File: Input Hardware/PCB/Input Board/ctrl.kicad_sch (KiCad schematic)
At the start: 38 parts

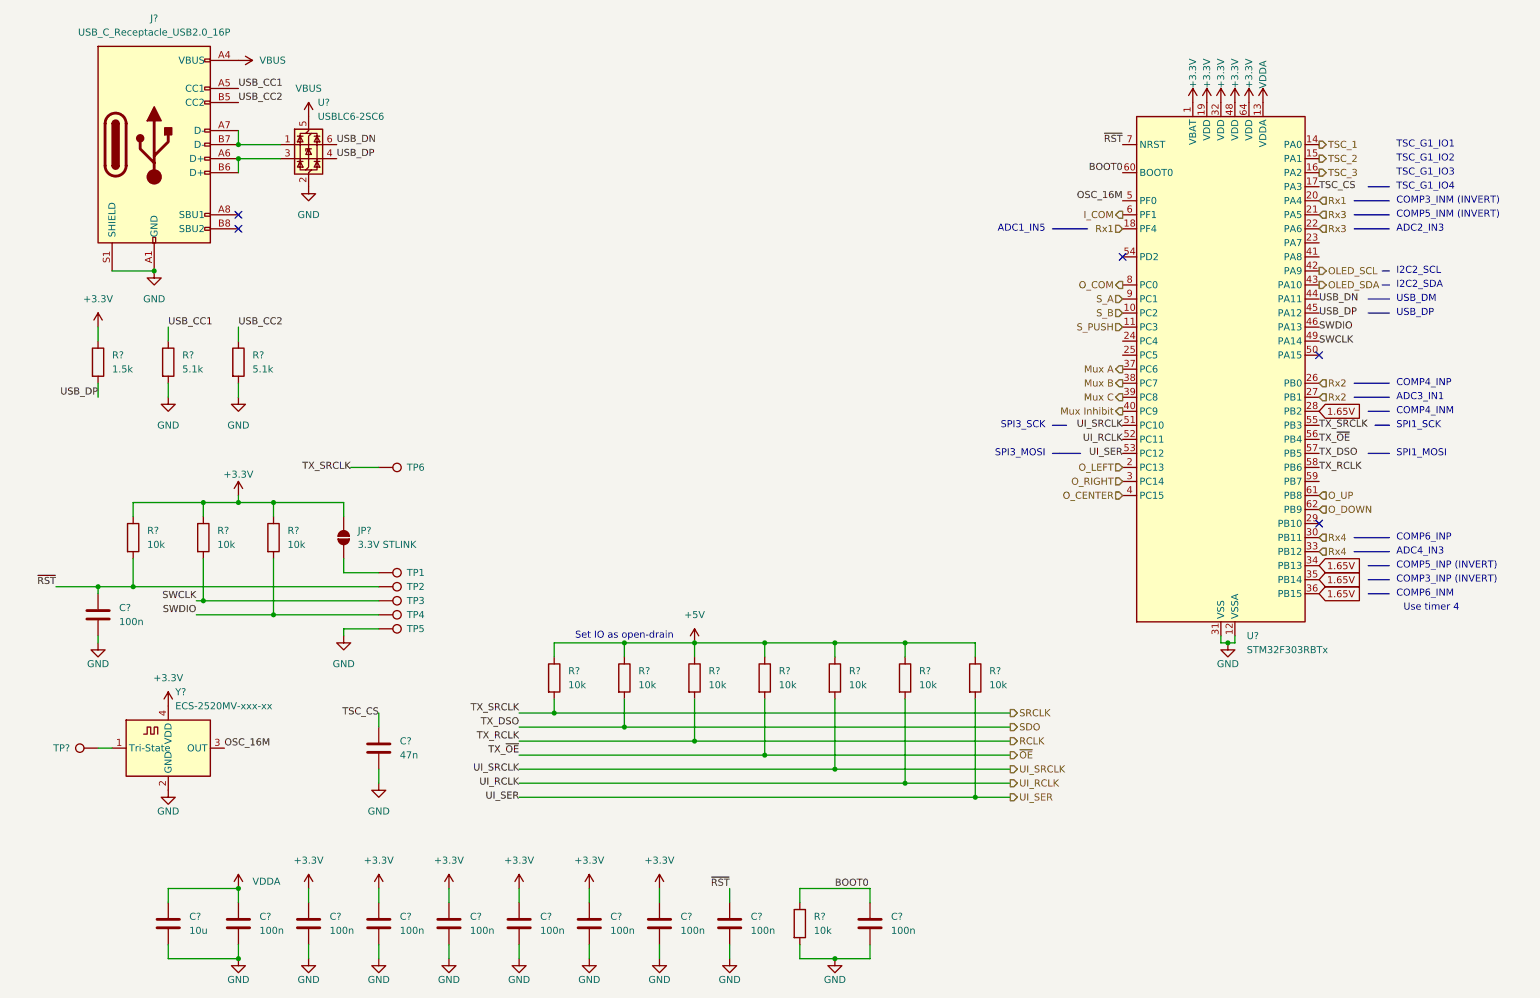
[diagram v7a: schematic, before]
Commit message: Add footprints
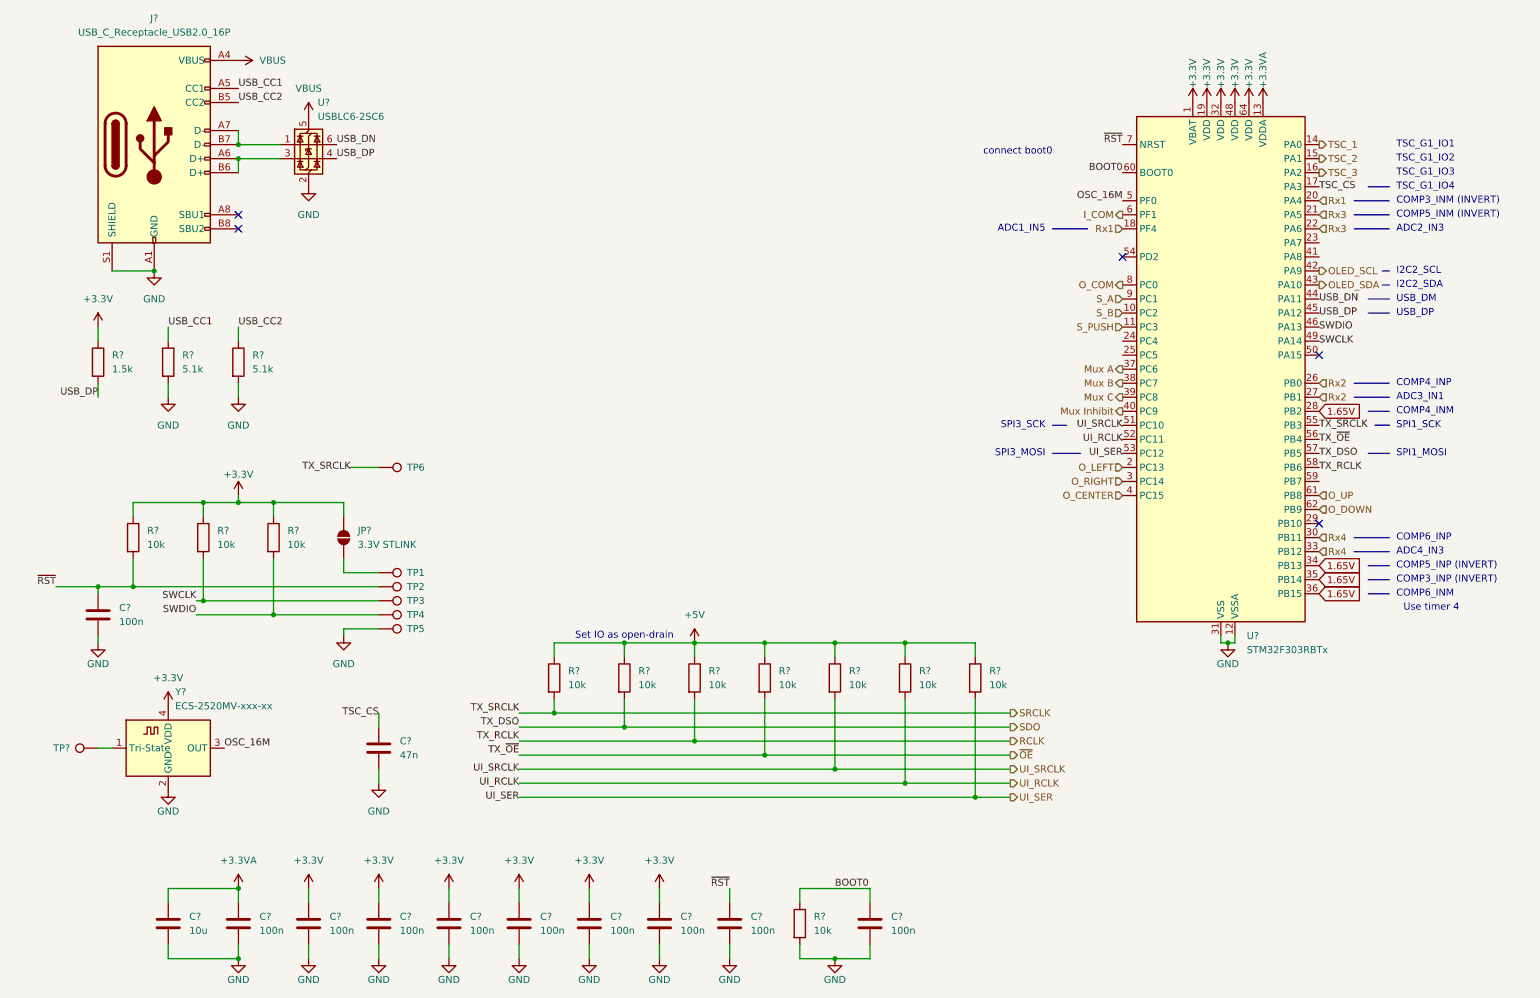
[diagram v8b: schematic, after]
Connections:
- net VDDA renamed +3.3VA
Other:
- note added: "connect boot0"
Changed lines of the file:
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@@
 		)
 	)
+	(text "connect boot0"
+		(exclude_from_sim no)
+		(at 198.12 44.45 0)
+		(effects
+			(font
+				(size 1.27 1.27)
+			)
+			(justify right)
+		)
+	)
 	(text "COMP4_INM"
 		(exclude_from_sim no)
@@
 	)
 	(junction
+		(at 50.8 177.8)
+		(diameter 0)
+		(color 0 0 0 0)
+	)
+	(junction
 		(at 50.8 107.95)
 		(diameter 0)
@@
 	)
 	(junction
-		(at 50.8 177.8)
-		(diameter 0)
-		(color 0 0 0 0)
-	)
-	(junction
 		(at 158.75 133.35)
 		(diameter 0)
@@
 	)
 	(symbol
+		(lib_id "power:+3.3VA")
+		(at 236.22 35.56 0)
+		(unit 1)
+		(exclude_from_sim no)
+		(in_bom yes)
+		(on_board yes)
+		(dnp no)
+		(property "Reference" "#PWR0137"
+			(at 236.22 39.37 0)
+			(effects
+				(font
+					(size 1.27 1.27)
+				)
+				(hide yes)
+			)
+		)
+		(property "Value" "+3.3VA"
+			(at 236.22 33.02 90)
+			(effects
+				(font
+					(size 1.27 1.27)
+				)
+				(justify left)
+			)
+		)
+		(property "Footprint" ""
+			(at 236.22 35.56 0)
+			(effects
+				(font
+					(size 1.27 1.27)
+				)
+				(hide yes)
+			)
+		)
+		(property "Datasheet" ""
+			(at 236.22 35.56 0)
+			(effects
+				(font
+					(size 1.27 1.27)
+				)
+				(hide yes)
+			)
+		)
+		(property "Description" "Power symbol creates a global label with name \"+3.3VA\""
+			(at 236.22 35.56 0)
+			(effects
+				(font
+					(size 1.27 1.27)
+				)
+				(hide yes)
+			)
+		)
+		(pin "1"
+		)
+		(instances
+			(project "Input Board"
+				(path "/198ad8d1-66e3-4deb-889c-1af2b81e67c3/5c16bd2e-d56c-40b8-b84c-f5532d41d46a"
+					(reference "#PWR0137")
+					(unit 1)
+				)
+			)
+		)
+	)
+	(symbol
 		(lib_id "Device:R")
 		(at 50.8 82.55 0)
@@
 	)
 	(symbol
+		(lib_id "power:+3.3VA")
+		(at 50.8 177.8 0)
+		(unit 1)
+		(exclude_from_sim no)
+		(in_bom yes)
+		(on_board yes)
+		(dnp no)
+		(fields_autoplaced yes)
+		(property "Reference" "#PWR0139"
+			(at 50.8 181.61 0)
+			(effects
+				(font
+					(size 1.27 1.27)
+				)
+				(hide yes)
+			)
+		)
+		(property "Value" "+3.3VA"
+			(at 50.8 172.72 0)
+			(effects
+				(font
+					(size 1.27 1.27)
+				)
+			)
+		)
+		(property "Footprint" ""
+			(at 50.8 177.8 0)
+			(effects
+				(font
+					(size 1.27 1.27)
+				)
+				(hide yes)
+			)
+		)
+		(property "Datasheet" ""
+			(at 50.8 177.8 0)
+			(effects
+				(font
+					(size 1.27 1.27)
+				)
+				(hide yes)
+			)
+		)
+		(property "Description" "Power symbol creates a global label with name \"+3.3VA\""
+			(at 50.8 177.8 0)
+			(effects
+				(font
+					(size 1.27 1.27)
+				)
+				(hide yes)
+			)
+		)
+		(pin "1"
+		)
+		(instances
+			(project "Input Board"
+				(path "/198ad8d1-66e3-4deb-889c-1af2b81e67c3/5c16bd2e-d56c-40b8-b84c-f5532d41d46a"
+					(reference "#PWR0139")
+					(unit 1)
+				)
+			)
+		)
+	)
+	(symbol
 		(lib_id "power:VBUS")
 		(at 50.8 27.94 270)
@@
 	)
 	(symbol
-		(lib_id "power:+3.3VA")
-		(at 50.8 177.8 0)
-		(unit 1)
-		(exclude_from_sim no)
-		(in_bom yes)
-		(on_board yes)
-		(dnp no)
-		(fields_autoplaced yes)
-		(property "Reference" "#PWR0199"
-			(at 50.8 181.61 0)
-			(effects
-				(font
-					(size 1.27 1.27)
-				)
-				(hide yes)
-			)
-		)
-		(property "Value" "VDDA"
-			(at 53.34 176.5299 0)
-			(effects
-				(font
-					(size 1.27 1.27)
-				)
-				(justify left)
-			)
-		)
-		(property "Footprint" ""
-			(at 50.8 177.8 0)
-			(effects
-				(font
-					(size 1.27 1.27)
-				)
-				(hide yes)
-			)
-		)
-		(property "Datasheet" ""
-			(at 50.8 177.8 0)
-			(effects
-				(font
-					(size 1.27 1.27)
-				)
-				(hide yes)
-			)
-		)
-		(property "Description" "Power symbol creates a global label with name \"+3.3VA\""
-			(at 50.8 177.8 0)
-			(effects
-				(font
-					(size 1.27 1.27)
-				)
-				(hide yes)
-			)
-		)
-		(pin "1"
-		)
-		(instances
-			(project ""
-				(path "/198ad8d1-66e3-4deb-889c-1af2b81e67c3/5c16bd2e-d56c-40b8-b84c-f5532d41d46a"
-					(reference "#PWR0199")
-					(unit 1)
-				)
-			)
-		)
-	)
-	(symbol
 		(lib_id "power:GND")
 		(at 101.6 190.5 0)
@@
 					(unit 1)
 				)
-			)
-		)
-	)
-	(symbol
-		(lib_id "power:+3.3VA")
-		(at 236.22 35.56 0)
-		(unit 1)
-		(exclude_from_sim no)
-		(in_bom yes)
-		(on_board yes)
-		(dnp no)
-		(property "Reference" "#PWR0186"
-			(at 236.22 39.37 0)
-			(effects
-				(font
-					(size 1.27 1.27)
-				)
-				(hide yes)
-			)
-		)
-		(property "Value" "VDDA"
-			(at 236.22 33.02 90)
-			(effects
-				(font
-					(size 1.27 1.27)
-				)
-				(justify left)
-			)
-		)
-		(property "Footprint" ""
-			(at 236.22 35.56 0)
-			(effects
-				(font
-					(size 1.27 1.27)
-				)
-				(hide yes)
-			)
-		)
-		(property "Datasheet" ""
-			(at 236.22 35.56 0)
-			(effects
-				(font
-					(size 1.27 1.27)
-				)
-				(hide yes)
-			)
-		)
-		(property "Description" "Power symbol creates a global label with name \"+3.3VA\""
-			(at 236.22 35.56 0)
-			(effects
-				(font
-					(size 1.27 1.27)
-				)
-				(hide yes)
-			)
-		)
-		(pin "1"
-		)
-		(instances
-			(project "Input Board"
-				(path "/198ad8d1-66e3-4deb-889c-1af2b81e67c3/5c16bd2e-d56c-40b8-b84c-f5532d41d46a"
-					(reference "#PWR0186")
-					(unit 1)
-				)
